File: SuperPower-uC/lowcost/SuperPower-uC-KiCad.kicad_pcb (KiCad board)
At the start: 2 copper layers, 81 x 28.5 mm, 81 parts, among them J1 Battery connector, J2 Thermistor, J3 USB_B_Micro, J4 Solar in, J5 main pin header fight, J6 main pin header left, Q1 2N7002, Q2 2N7002, Q3 S8050, Q4 S8050, Q5 AO3401A, Q6 AO3401A, Q7 2N7002, U1 FS312F-G, U10 FP6291LR, U11 ME6210A33P, U12 ME6210A33P, U13 ESP32-WROOM32, U2 FS8205A, U3 LC709203FQH, U4 TP4056, U5 CH340G, U6 AMS1117-3.3, U7 PCF8563T, U8 XC6206P332MR, U9 TCA6408A, Y1 12MHZ, Y2 32.768KHz

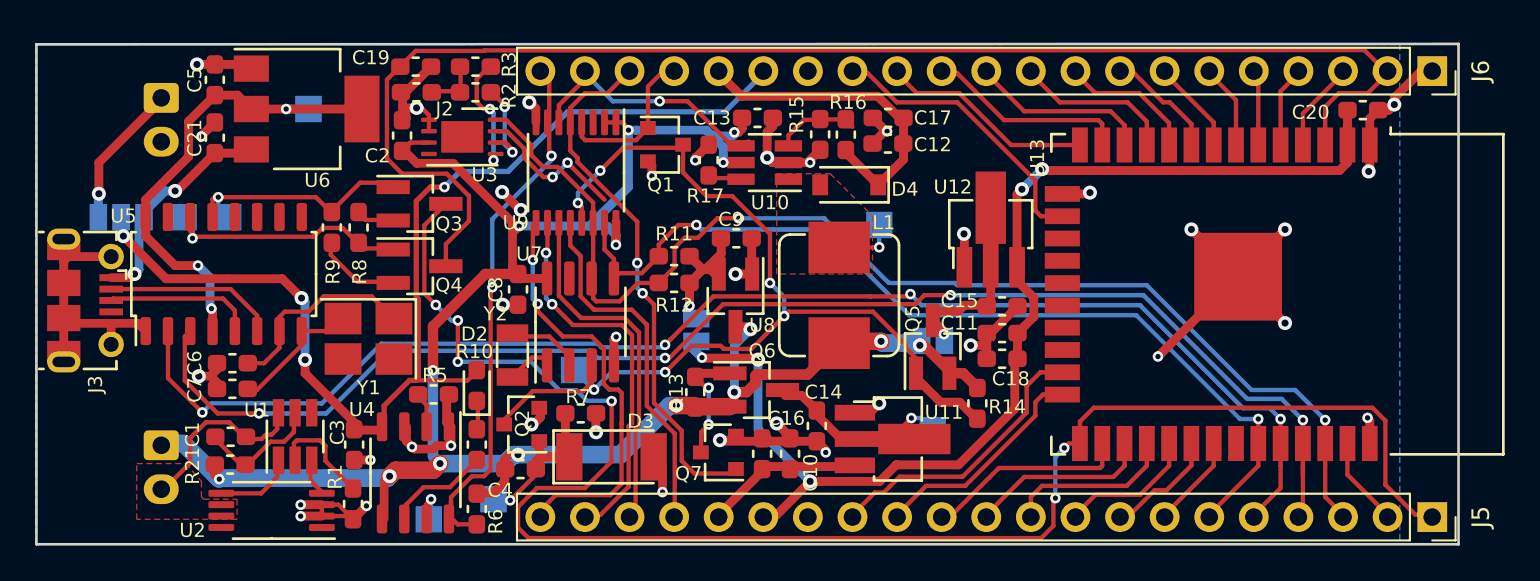
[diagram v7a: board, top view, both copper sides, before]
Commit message: edited header footprint to get rid of drc (with good reason)
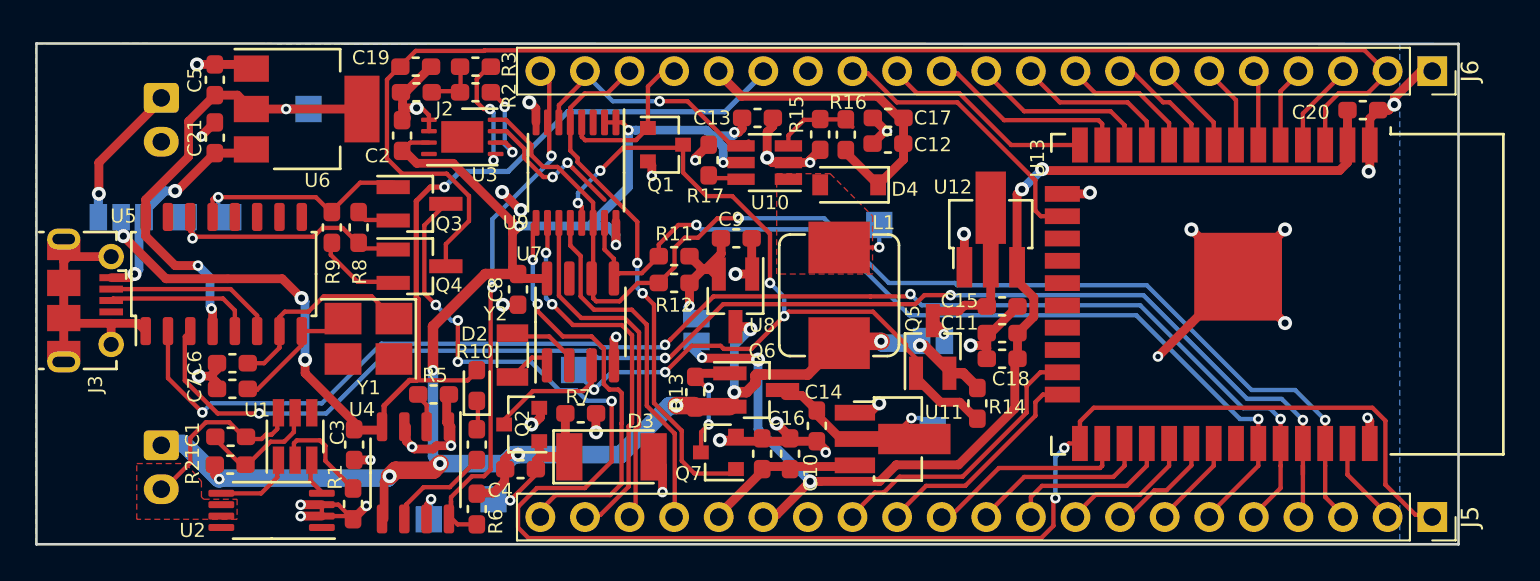
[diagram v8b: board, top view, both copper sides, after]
